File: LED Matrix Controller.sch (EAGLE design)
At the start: 7 parts, among them J1 5V PWR, J2 LED OUT, J4 SER DBG

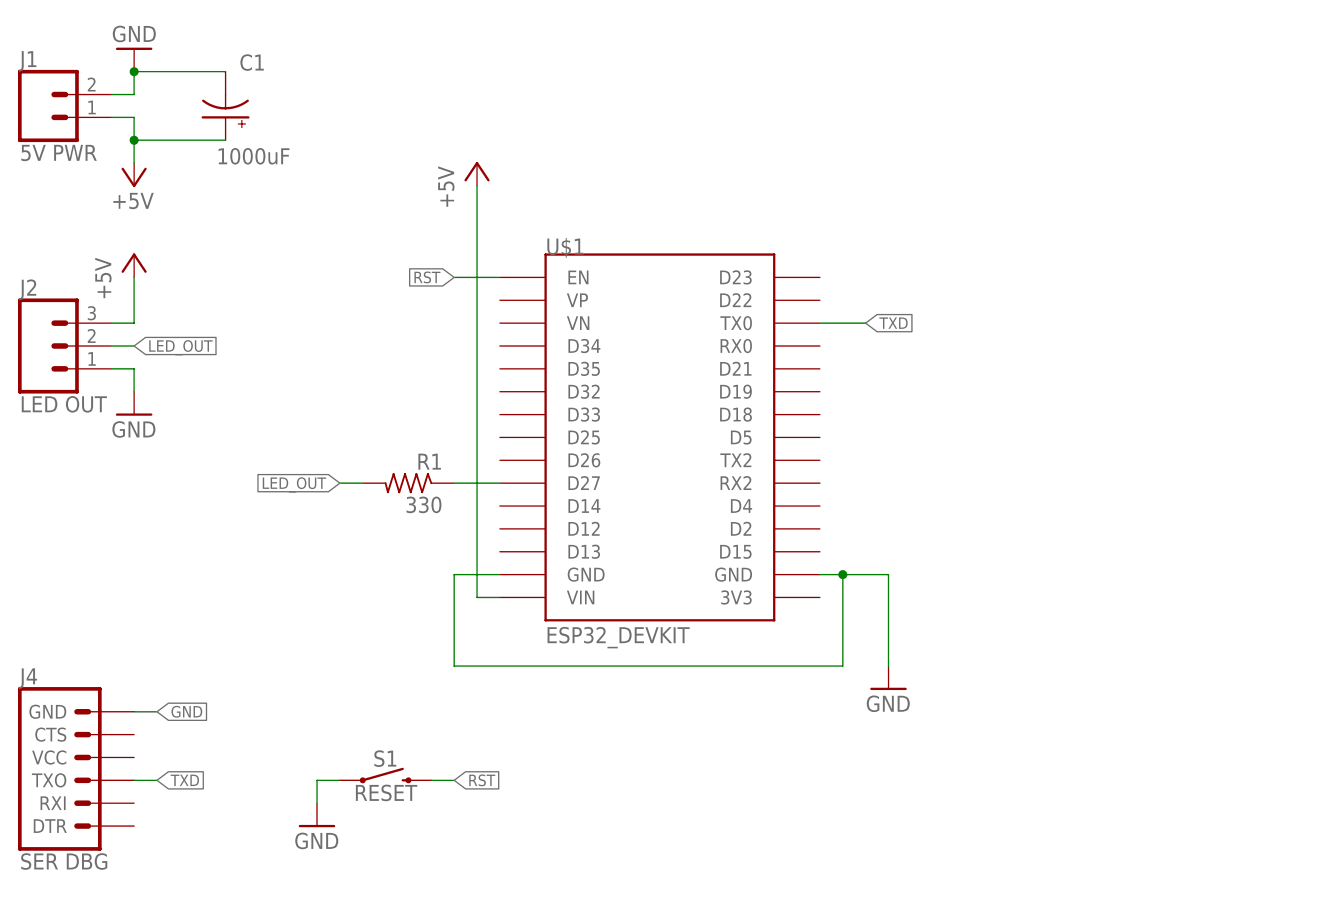
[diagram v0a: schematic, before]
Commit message: Add a 74HCT245 as a level shifter
The ESP32 uses 3.3v logic, and even though it "worked" on my test
board, it's possible that I was just lucky. The Internet wants me to
use this chip, even though I'm wasting 7 buffers for a single I/O.

I'd like to build up one of these, but I will probably change it later
for something smaller.
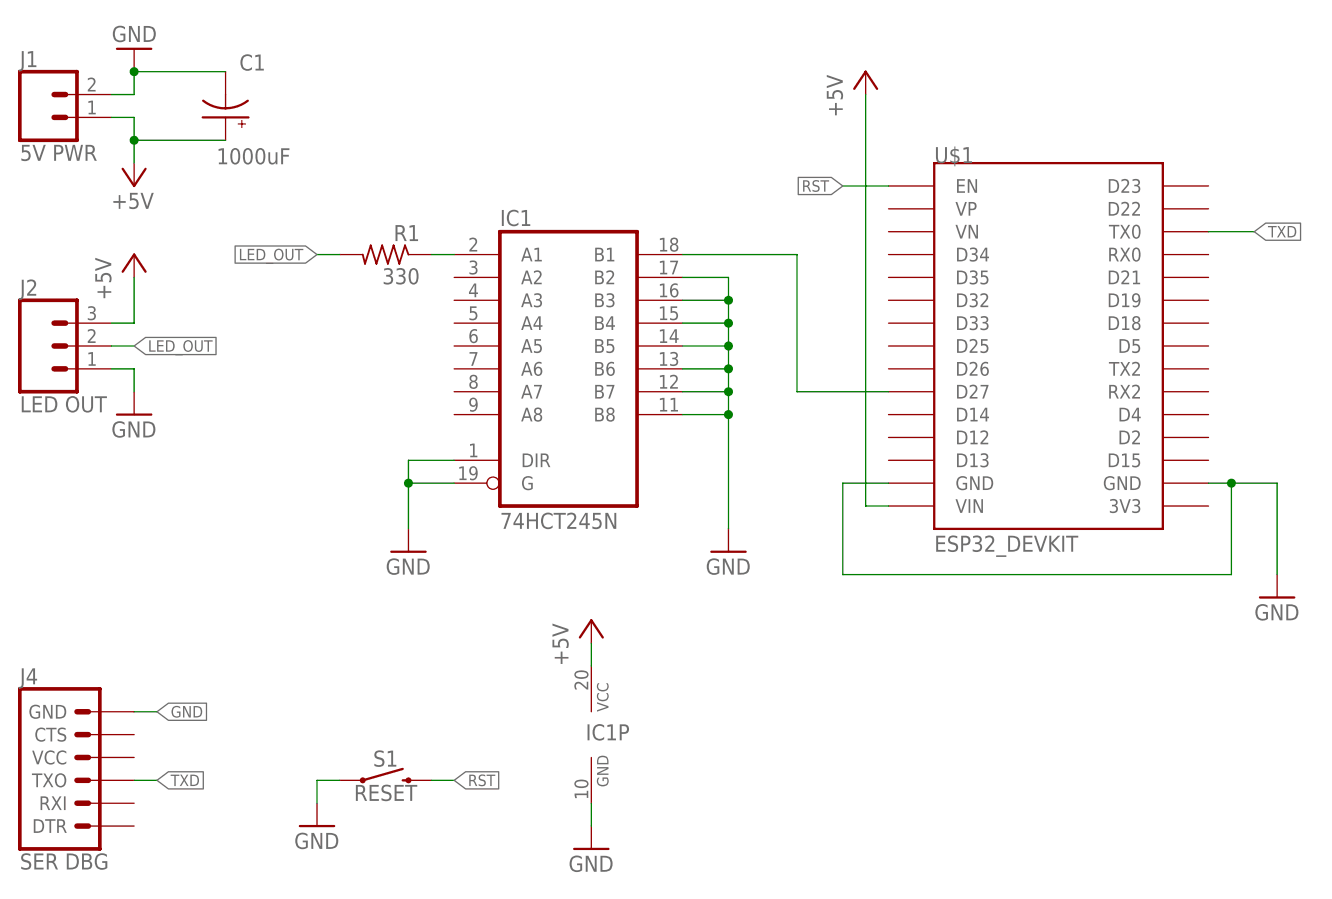
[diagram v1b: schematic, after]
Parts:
- added IC1: 74HCT245N, 74xx-eu:74HCT245N
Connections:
- new net N$2: IC1A.A1, R1.1
- net +5V: now also IC1P.VCC
- net GND: now also IC1A.B2, IC1A.B3, IC1A.B4, IC1A.B5, IC1A.B6, IC1A.B7, IC1A.B8, IC1A.DIR, IC1A.G, IC1P.GND
- net N$1: now also IC1A.B1; no longer R1.1
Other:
- moved on the sheet: R1, U$1
